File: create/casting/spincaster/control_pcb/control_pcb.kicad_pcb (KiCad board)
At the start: 2 copper layers, 78.7 x 53.3 mm, 10 parts, among them J1 Extra, J2 Buzzer, J3 Relay, J4 FET, J5 Rocker, J6 PWR, SW2 IND_OFF, SW3 IND_ON, SW4 IND_PULSE

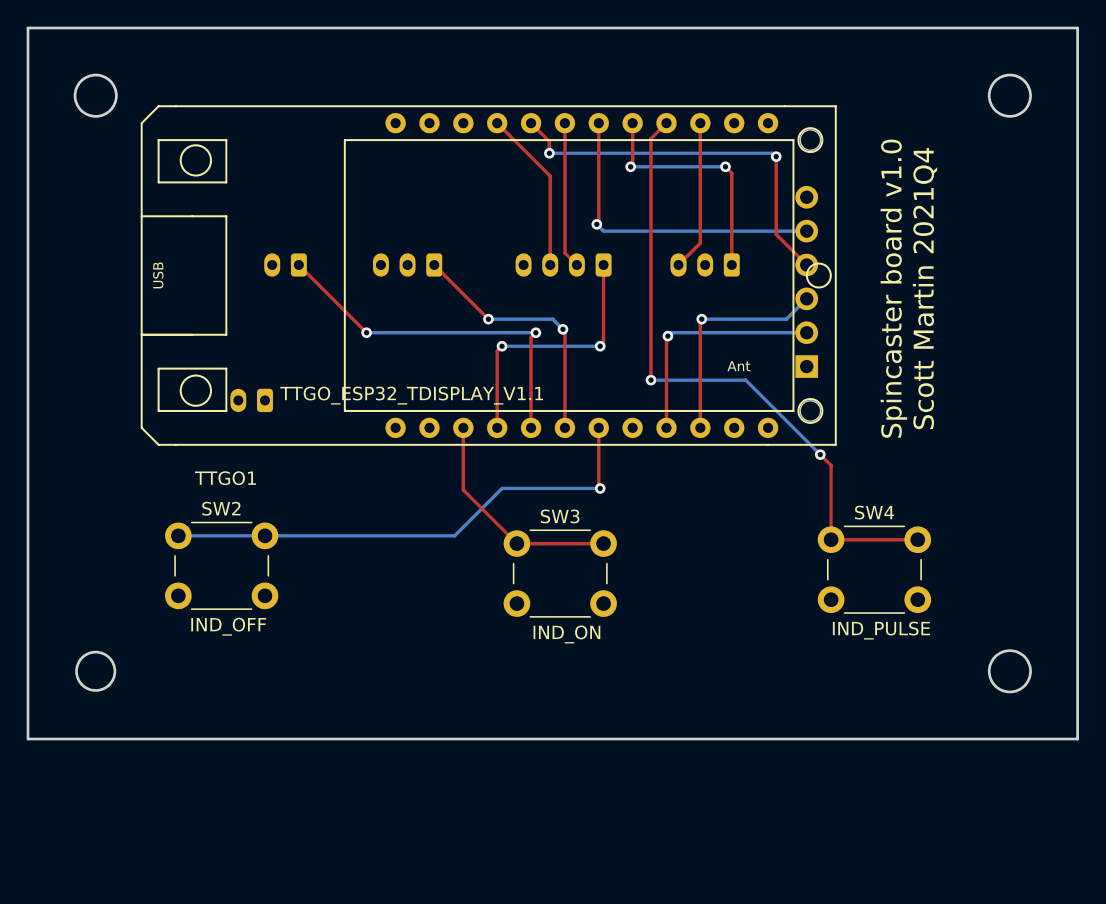
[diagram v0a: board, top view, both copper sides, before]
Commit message: Better touch-mark, added mixer float notebook, some mods to spincaster control
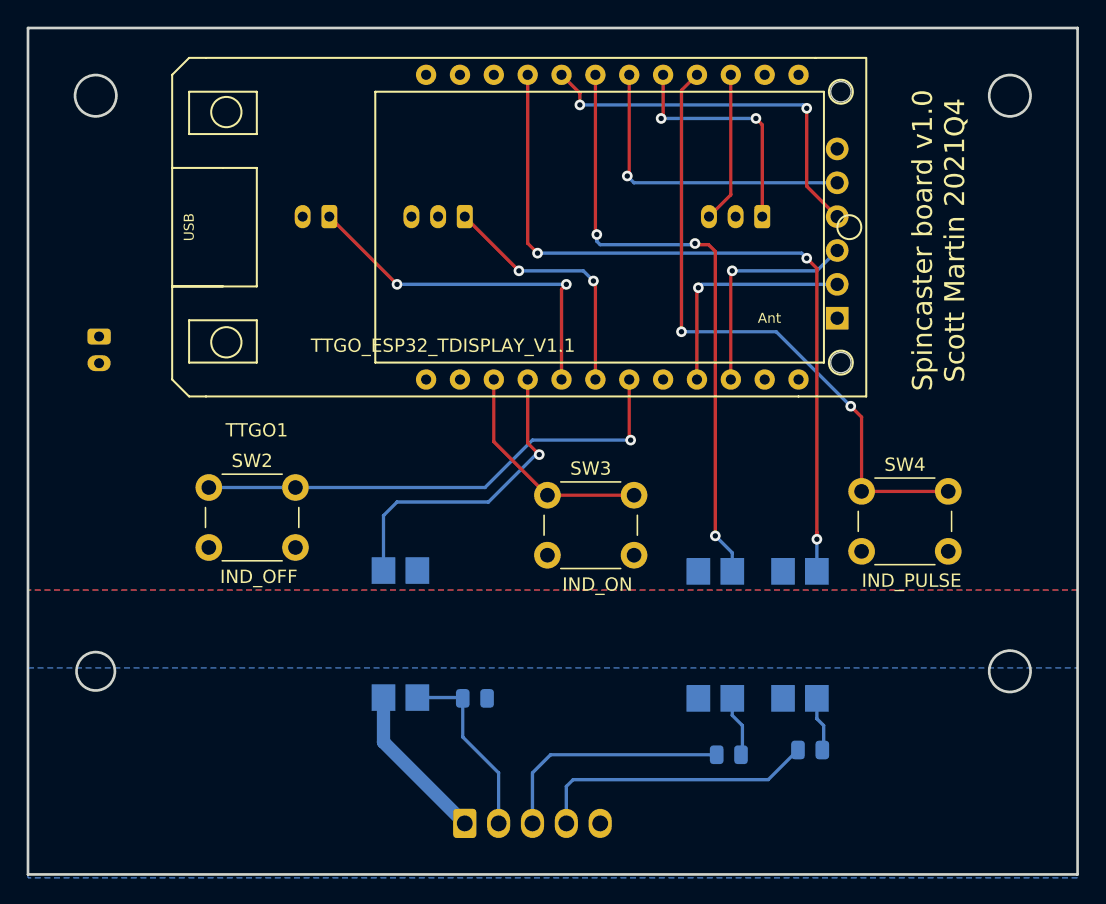
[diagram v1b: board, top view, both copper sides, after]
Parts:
- added R1: R_US, Resistor_SMD:R_0805_2012Metric, B.Cu at (154.2, 130.7)
- added R2: R_US, Resistor_SMD:R_0805_2012Metric, B.Cu at (160.3, 130.4)
- added R3: R_US, Resistor_SMD:R_0805_2012Metric, B.Cu at (135.1, 126.5)
- added U1: LTV-817S, Package_DIP:SMDIP-4_W9.53mm, B.Cu at (153.2, 121.7)
- added U2: LTV-817S, Package_DIP:SMDIP-4_W9.53mm, B.Cu at (159.5, 121.7)
- added U3: LTV-817S, Package_DIP:SMDIP-4_W9.53mm, B.Cu at (129.5, 121.7)
- J4: value FET -> Conn_01x05_Female; footprint Connector_JST:JST_PH_B4B-PH-K_1x04_P2.00mm_Vertical -> Connector_Molex:Molex_KK-254_AE-6410-05A_1x05_P2.54mm_Vertical
- moved J4 43.2 mm to (134.4, 135.9), turned to 0 degrees
- moved J6 13.3 mm to (106.9, 99.3), turned to -90 degrees
- moved J1 4.29 mm to (162.3, 98.0)
- moved J2 4.29 mm to (124.2, 90.4)
- moved J3 4.29 mm to (134.4, 90.4)
- moved J5 4.29 mm to (156.7, 90.4)
- moved SW2 4.29 mm to (115.2, 110.7)
- moved SW3 4.29 mm to (140.6, 111.3)
- moved SW4 4.29 mm to (164.1, 111.0)
- moved TTGO1 4.29 mm to (115.0, 103.8)
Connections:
- net VCC renamed VDD
- J1 pad 6: GND -> GNDD
- J2 pad 2: GND -> GNDD
- J3 pad 3: GND -> GNDD
- J4 pad 1: /FET -> +BATT
- J4 pad 2: /SW_LID -> /DRL_FET
- J4 pad 3: /SW_SPIN -> /DRL_LID
- J4 pad 4: GND -> /DRL_SPIN
- J5 pad 2: GND -> GNDD
- J6 pad 2: GND -> GNDD
- SW2 pad 2: GND -> GNDD
- SW3 pad 2: GND -> GNDD
- SW4 pad 2: GND -> GNDD
- TTGO1 pad 13: GND -> GNDD
- TTGO1 pad 14: GND -> GNDD
- TTGO1 pad 2: GND -> GNDD
- TTGO1 pad 22: GND -> GNDD
- TTGO1 pad 23: GND -> GNDD
- TTGO1 pad 4: /FET -> /FET_OUT
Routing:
- net /SW_SPIN: track 12.3 -> 57.8 mm, vias 0 -> 3
- net /SW_LID: track 11.0 -> 46.3 mm, vias 0 -> 3
- net /FET_OUT: track 0.00 -> 23.7 mm, vias 0 -> 1
- net /DRL_SPIN: track 0.00 -> 21.3 mm
- net /FET: track 20.0 -> 0.00 mm, vias 2 -> 0
- net /DRL_LID: track 0.00 -> 18.2 mm
- net /DRL_FET: track 0.00 -> 13.9 mm
- net +BATT: track 0.00 -> 12.0 mm
- net Net-(R1-Pad2): track 0.00 -> 4.59 mm
- net Net-(R2-Pad2): track 0.00 -> 4.12 mm
- added copper zone on B.Cu, net GNDD
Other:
- board size 78.7 x 53.3 mm -> 78.7 x 63.5 mm
